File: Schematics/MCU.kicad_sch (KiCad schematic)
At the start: 0 parts

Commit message: Selected MCU
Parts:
- added U?: ATmega32U4-M, Package_DFN_QFN:QFN-44-1EP_7x7mm_P0.5mm_EP5.2x5.2mm, symbol MCU_Microchip_ATmega:ATmega32U4-M
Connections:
- new net: U?.14 (VCC), U?.34 (VCC)
- new net: U?.15 (GND), U?.23 (GND), U?.35 (GND), U?.43 (GND), U?.45 (GND)
- new net: U?.24 (AVCC), U?.44 (AVCC)
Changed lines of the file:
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@@
 (kicad_sch (version 20211123) (generator eeschema)
   (paper "A4")
+  (symbol (lib_id "MCU_Microchip_ATmega:ATmega32U4-M") (at 147.32 101.6 0) (unit 1)
+    (in_bom yes) (on_board yes) (fields_autoplaced)
+    (property "Reference" "U?" (id 0) (at 149.3394 146.9295 0)
+      (effects (font (size 1.27 1.27)) (justify left))
+    )
+    (property "Value" "ATmega32U4-M" (id 1) (at 149.3394 149.7046 0)
+      (effects (font (size 1.27 1.27)) (justify left))
+    )
+    (property "Footprint" "Package_DFN_QFN:QFN-44-1EP_7x7mm_P0.5mm_EP5.2x5.2mm" (id 2) (at 147.32 101.6 0)
+      (effects (font (size 1.27 1.27) italic) hide)
+    )
+    (property "Datasheet" "http://ww1.microchip.com/downloads/en/DeviceDoc/Atmel-7766-8-bit-AVR-ATmega16U4-32U4_Datasheet.pdf" (id 3) (at 147.32 101.6 0)
+      (effects (font (size 1.27 1.27)) hide)
+    )
+    (pin "1")
+    (pin "10")
+    (pin "11")
+    (pin "12")
+    (pin "13")
+    (pin "14")
+    (pin "15")
+    (pin "16")
+    (pin "17")
+    (pin "18")
+    (pin "19")
+    (pin "2")
+    (pin "20")
+    (pin "21")
+    (pin "22")
+    (pin "23")
+    (pin "24")
+    (pin "25")
+    (pin "26")
+    (pin "27")
+    (pin "28")
+    (pin "29")
+    (pin "3")
+    (pin "30")
+    (pin "31")
+    (pin "32")
+    (pin "33")
+    (pin "34")
+    (pin "35")
+    (pin "36")
+    (pin "37")
+    (pin "38")
+    (pin "39")
+    (pin "4")
+    (pin "40")
+    (pin "41")
+    (pin "42")
+    (pin "43")
+    (pin "44")
+    (pin "45")
+    (pin "5")
+    (pin "6")
+    (pin "7")
+    (pin "8")
+    (pin "9")
+  )
 )

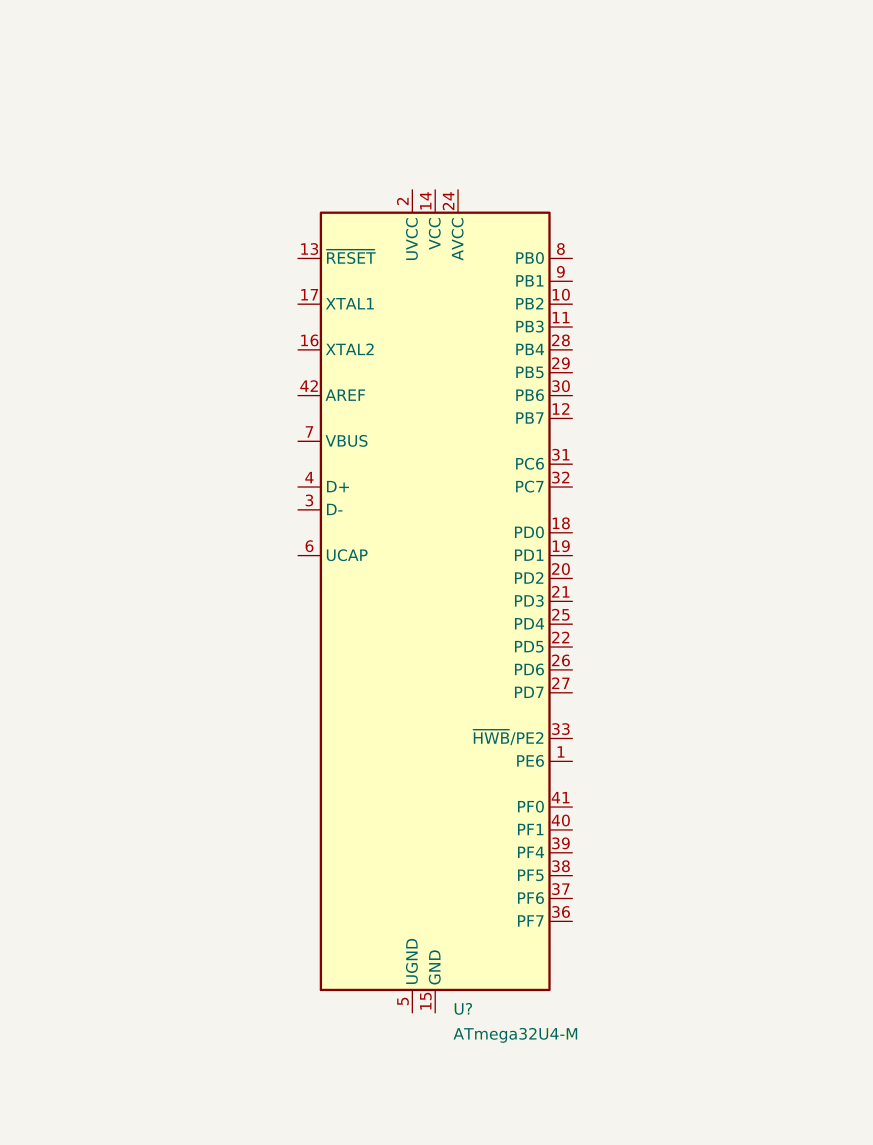
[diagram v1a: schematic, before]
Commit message: Add MCU circuit
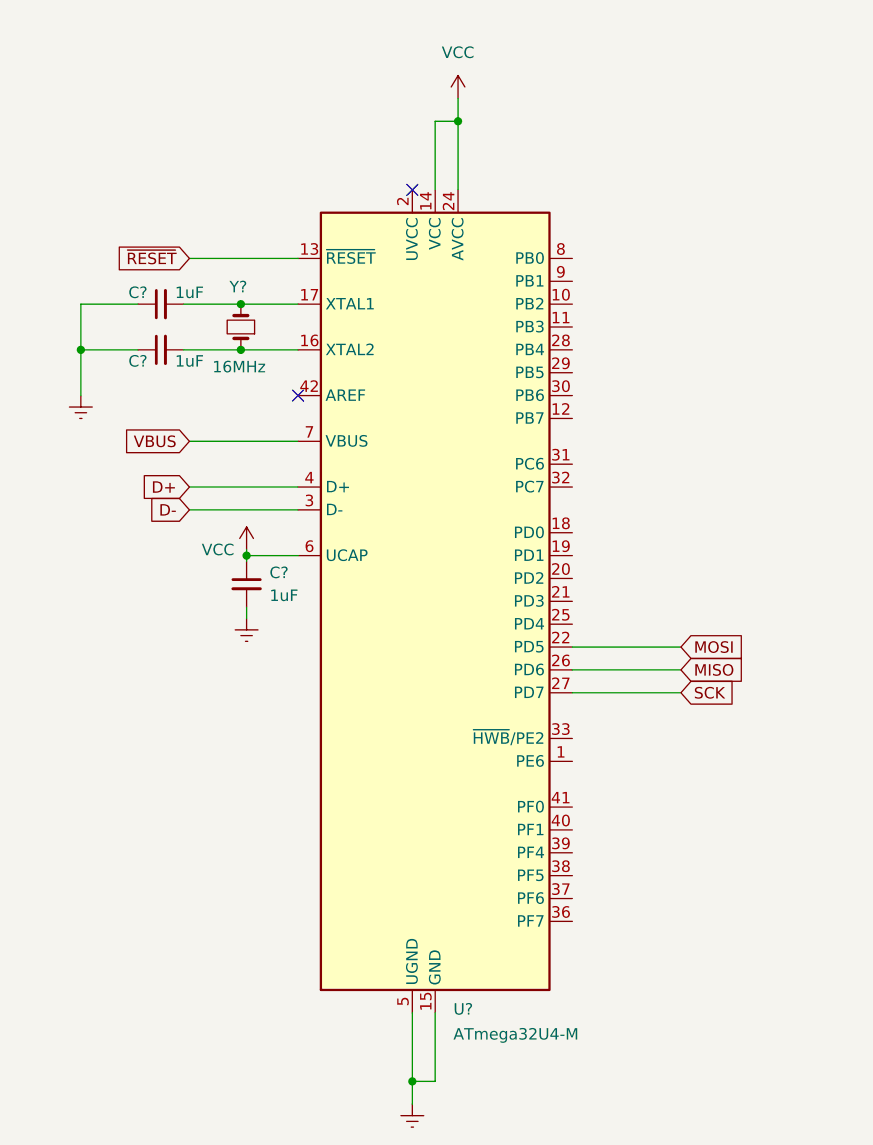
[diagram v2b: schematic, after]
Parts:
- added C? (x3): 1uF, symbol Device:C_Small
- added Y?: 16MHz, symbol Device:Crystal_Small
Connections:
- net ~{RESET}: now reaches U?.13 (~{RESET})
- net VCC: now reaches U?.14 (VCC), U?.34 (VCC)
- net VCC: now also U?.24 (AVCC), U?.44 (AVCC), U?.6 (UCAP), C?.1
- net Earth: now reaches U?.15 (GND), U?.23 (GND), U?.35 (GND), U?.43 (GND), U?.45 (GND)
- net Earth: now also U?.5 (UGND), C?.1, C?.1, C?.2
- net at U?.16 (XTAL2): now also C?.2, Y?.1
- net at U?.17 (XTAL1): now also C?.2, Y?.2
- net MOSI: now reaches U?.22 (PD5)
- net MISO: now reaches U?.26 (PD6)
- net SCK: now reaches U?.27 (PD7)
- net D-: now reaches U?.3 (D-)
- net D+: now reaches U?.4 (D+)
- net VBUS: now reaches U?.7 (VBUS)
- no-connect marks 0 -> 2

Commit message: Changed MCU
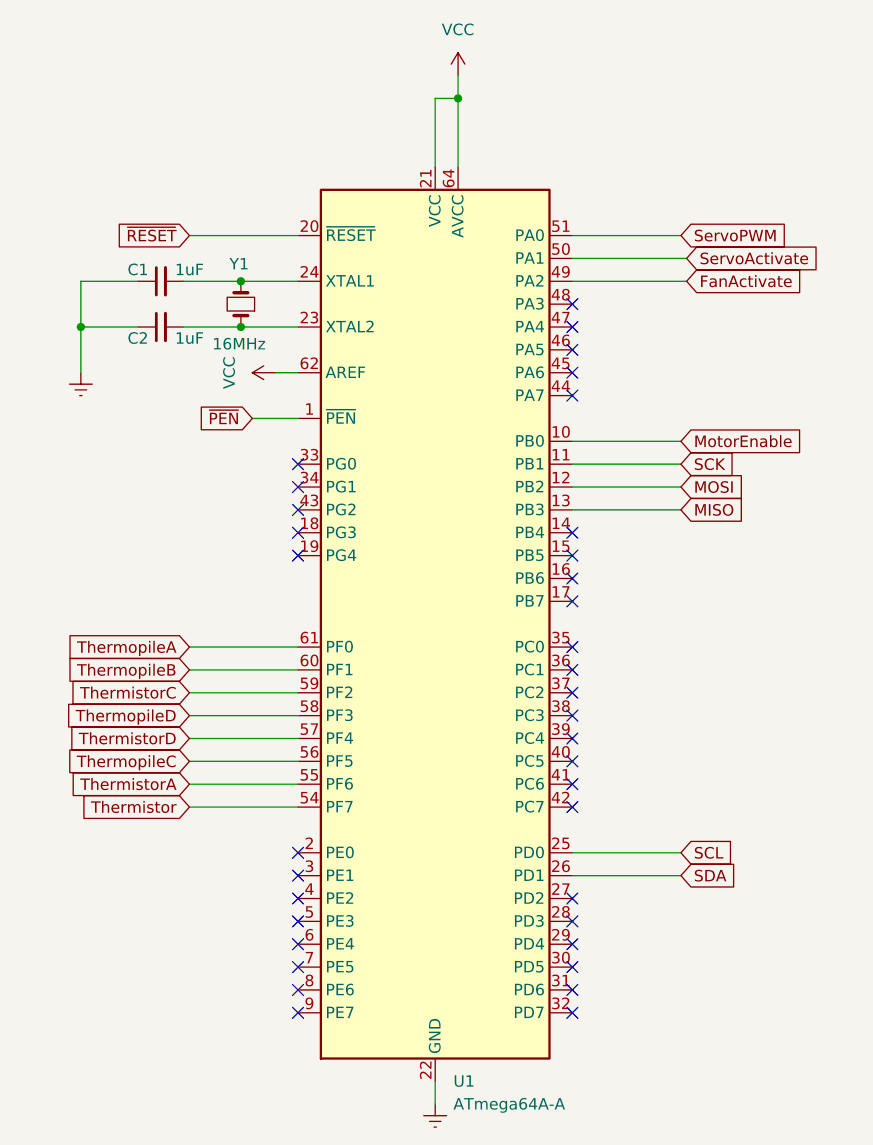
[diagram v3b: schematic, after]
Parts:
- removed C? (x3): 1uF, symbol Device:C_Small
- removed U?: ATmega32U4-M, Package_DFN_QFN:QFN-44-1EP_7x7mm_P0.5mm_EP5.2x5.2mm, symbol MCU_Microchip_ATmega:ATmega32U4-M
- removed Y?: 16MHz, symbol Device:Crystal_Small
- added C1, C2: 1uF, symbol Device:C_Small
- added U1: ATmega64A-A, Package_QFP:TQFP-64_14x14mm_P0.8mm, symbol MCU_Microchip_ATmega:ATmega64A-A
- added Y1: 16MHz, symbol Device:Crystal_Small
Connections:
- net Earth: now also C1.1, C2.1, U1.22 (GND), U1.53 (GND), U1.63 (GND)
- net MISO: now also U1.13 (PB3)
- net MOSI: now also U1.12 (PB2)
- net SCK: now also U1.11 (PB1)
- net VCC: now also U1.21 (VCC), U1.52 (VCC), U1.62 (AREF), U1.64 (AVCC)
- net ~{RESET}: now also U1.20 (~{RESET})
- new net: C2.2, U1.23 (XTAL2), Y1.1
- new net: C1.2, U1.24 (XTAL1), Y1.2
- new net FanActivate: U1.49 (PA2)
- new net MotorEnable: U1.10 (PB0)
- new net SCL: U1.25 (PD0)
- new net SDA: U1.26 (PD1)
- new net ServoActivate: U1.50 (PA1)
- new net ServoPWM: U1.51 (PA0)
- new net Thermistor: U1.54 (PF7)
- new net ThermistorA: U1.55 (PF6)
- new net ThermistorC: U1.59 (PF2)
- new net ThermistorD: U1.57 (PF4)
- new net ThermopileA: U1.61 (PF0)
- new net ThermopileB: U1.60 (PF1)
- new net ThermopileC: U1.56 (PF5)
- new net ThermopileD: U1.58 (PF3)
- new net ~{PEN}: U1.1 (~{PEN})
- no-connect marks 2 -> 36

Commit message: Added Footprints
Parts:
- C1, C2: footprint (none) -> Resistor_SMD:R_0603_1608Metric_Pad0.98x0.95mm_HandSolder
- Y1: footprint (none) -> SFRFootprints:XTAL_ECS-160-S-23A-TR
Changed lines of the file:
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@@
       (effects (font (size 1.27 1.27)) (justify right))
     )
-    (property "Footprint" "" (id 2) (at 125.73 68.58 0)
+    (property "Footprint" "SFRFootprints:XTAL_ECS-160-S-23A-TR" (id 2) (at 125.73 68.58 0)
       (effects (font (size 1.27 1.27)) hide)
     )
@@
     (property "Reference" "C2" (id 0) (at 114.3 72.39 90))
     (property "Value" "1uF" (id 1) (at 120.015 72.39 90))
-    (property "Footprint" "" (id 2) (at 116.84 71.12 0)
+    (property "Footprint" "Resistor_SMD:R_0603_1608Metric_Pad0.98x0.95mm_HandSolder" (id 2) (at 116.84 71.12 0)
       (effects (font (size 1.27 1.27)) hide)
     )
@@
     (property "Reference" "C1" (id 0) (at 114.3 64.77 90))
     (property "Value" "1uF" (id 1) (at 120.015 64.77 90))
-    (property "Footprint" "" (id 2) (at 116.84 66.04 0)
+    (property "Footprint" "Resistor_SMD:R_0603_1608Metric_Pad0.98x0.95mm_HandSolder" (id 2) (at 116.84 66.04 0)
       (effects (font (size 1.27 1.27)) hide)
     )

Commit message: PCB
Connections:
- net ThermistorA is gone; now on net ThermopileB: U1.55 (PF6)
- net Thermistor: now also U1.57 (PF4); no longer U1.54 (PF7)
- net ThermistorC: now also U1.60 (PF1); no longer U1.59 (PF2)
- net ThermistorD: now also U1.61 (PF0); no longer U1.57 (PF4)
- net ThermopileA: now also U1.56 (PF5); no longer U1.61 (PF0)
- net ThermopileB: no longer U1.60 (PF1)
- net ThermopileC: now also U1.59 (PF2); no longer U1.56 (PF5)
- new net ThermistorB: U1.54 (PF7)
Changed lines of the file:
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@@
   (no_connect (at 162.56 68.58))
   (no_connect (at 162.56 71.12))
+  (wire (pts (xy 118.11 109.22) (xy 132.08 109.22))
+    (stroke (width 0) (type default) (color 0 0 0 0))
+  )
   (wire (pts (xy 162.56 88.9) (xy 174.625 88.9))
     (stroke (width 0) (type default) (color 0 0 0 0))
   )
+  (wire (pts (xy 118.11 106.68) (xy 132.08 106.68))
+    (stroke (width 0) (type default) (color 0 0 0 0))
+  )
   (wire (pts (xy 107.95 71.12) (xy 107.95 76.2))
     (stroke (width 0) (type default) (color 0 0 0 0))
@@
     (stroke (width 0) (type default) (color 0 0 0 0))
   )
-  (wire (pts (xy 120.015 109.22) (xy 132.08 109.22))
-    (stroke (width 0) (type default) (color 0 0 0 0))
-  )
   (wire (pts (xy 127 81.28) (xy 132.08 81.28))
     (stroke (width 0) (type default) (color 0 0 0 0))
   )
-  (wire (pts (xy 120.015 114.3) (xy 132.08 114.3))
-    (stroke (width 0) (type default) (color 0 0 0 0))
-  )
   (wire (pts (xy 149.86 45.72) (xy 147.32 45.72))
     (stroke (width 0) (type default) (color 0 0 0 0))
   )
+  (wire (pts (xy 118.11 111.76) (xy 132.08 111.76))
+    (stroke (width 0) (type default) (color 0 0 0 0))
+  )
   (wire (pts (xy 125.73 71.12) (xy 132.08 71.12))
     (stroke (width 0) (type default) (color 0 0 0 0))
@@
     (stroke (width 0) (type default) (color 0 0 0 0))
   )
-  (wire (pts (xy 120.015 111.76) (xy 132.08 111.76))
-    (stroke (width 0) (type default) (color 0 0 0 0))
-  )
-  (wire (pts (xy 120.015 119.38) (xy 132.08 119.38))
-    (stroke (width 0) (type default) (color 0 0 0 0))
-  )
   (wire (pts (xy 149.86 53.34) (xy 149.86 45.72))
     (stroke (width 0) (type default) (color 0 0 0 0))
   )
-  (wire (pts (xy 120.015 124.46) (xy 132.08 124.46))
-    (stroke (width 0) (type default) (color 0 0 0 0))
-  )
   (wire (pts (xy 162.56 91.44) (xy 174.625 91.44))
     (stroke (width 0) (type default) (color 0 0 0 0))
@@
     (stroke (width 0) (type default) (color 0 0 0 0))
   )
-  (wire (pts (xy 120.015 121.92) (xy 132.08 121.92))
-    (stroke (width 0) (type default) (color 0 0 0 0))
-  )
   (wire (pts (xy 162.56 66.04) (xy 175.26 66.04))
     (stroke (width 0) (type default) (color 0 0 0 0))
@@
     (stroke (width 0) (type default) (color 0 0 0 0))
   )
+  (wire (pts (xy 118.11 119.38) (xy 132.08 119.38))
+    (stroke (width 0) (type default) (color 0 0 0 0))
+  )
   (wire (pts (xy 119.38 66.04) (xy 125.73 66.04))
     (stroke (width 0) (type default) (color 0 0 0 0))
   )
-  (wire (pts (xy 120.015 116.84) (xy 132.08 116.84))
+  (wire (pts (xy 118.11 114.3) (xy 132.08 114.3))
+    (stroke (width 0) (type default) (color 0 0 0 0))
+  )
+  (wire (pts (xy 118.11 116.84) (xy 132.08 116.84))
     (stroke (width 0) (type default) (color 0 0 0 0))
   )
@@
     (stroke (width 0) (type default) (color 0 0 0 0))
   )
-  (wire (pts (xy 120.015 106.68) (xy 132.08 106.68))
+  (wire (pts (xy 118.11 124.46) (xy 132.08 124.46))
+    (stroke (width 0) (type default) (color 0 0 0 0))
+  )
+  (wire (pts (xy 118.11 121.92) (xy 132.08 121.92))
     (stroke (width 0) (type default) (color 0 0 0 0))
   )
@@
     (stroke (width 0) (type default) (color 0 0 0 0))
   )
-  (global_label "ThermistorD" (shape input) (at 120.015 116.84 180) (fields_autoplaced)
-    (effects (font (size 1.27 1.27)) (justify right))
-    (property "Intersheet References" "${INTERSHEET_REFS}" (id 0) (at 106.3533 116.9194 0)
+  (global_label "ThermistorD" (shape input) (at 118.11 106.68 180) (fields_autoplaced)
+    (effects (font (size 1.27 1.27)) (justify right))
+    (property "Intersheet References" "${INTERSHEET_REFS}" (id 0) (at 104.4483 106.7594 0)
       (effects (font (size 1.27 1.27)) (justify right) hide)
     )
@@
     )
   )
-  (global_label "ThermopileC" (shape input) (at 120.015 119.38 180) (fields_autoplaced)
-    (effects (font (size 1.27 1.27)) (justify right))
-    (property "Intersheet References" "${INTERSHEET_REFS}" (id 0) (at 105.9905 119.4594 0)
+  (global_label "ThermopileC" (shape input) (at 118.11 111.76 180) (fields_autoplaced)
+    (effects (font (size 1.27 1.27)) (justify right))
+    (property "Intersheet References" "${INTERSHEET_REFS}" (id 0) (at 104.0855 111.8394 0)
       (effects (font (size 1.27 1.27)) (justify right) hide)
     )
@@
     )
   )
-  (global_label "ThermopileA" (shape input) (at 120.015 106.68 180) (fields_autoplaced)
-    (effects (font (size 1.27 1.27)) (justify right))
-    (property "Intersheet References" "${INTERSHEET_REFS}" (id 0) (at 106.1719 106.7594 0)
-      (effects (font (size 1.27 1.27)) (justify right) hide)
-    )
-  )
   (global_label "ServoPWM" (shape input) (at 174.625 60.96 0) (fields_autoplaced)
     (effects (font (size 1.27 1.27)) (justify left))
@@
     )
   )
+  (global_label "ThermopileB" (shape input) (at 118.11 121.92 180) (fields_autoplaced)
+    (effects (font (size 1.27 1.27)) (justify right))
+    (property "Intersheet References" "${INTERSHEET_REFS}" (id 0) (at 104.0855 121.8406 0)
+      (effects (font (size 1.27 1.27)) (justify right) hide)
+    )
+  )
   (global_label "~{RESET}" (shape input) (at 120.015 60.96 180) (fields_autoplaced)
     (effects (font (size 1.27 1.27)) (justify right))
@@
     )
   )
-  (global_label "ThermistorC" (shape input) (at 120.015 111.76 180) (fields_autoplaced)
-    (effects (font (size 1.27 1.27)) (justify right))
-    (property "Intersheet References" "${INTERSHEET_REFS}" (id 0) (at 106.3533 111.6806 0)
-      (effects (font (size 1.27 1.27)) (justify right) hide)
-    )
-  )
-  (global_label "ThermopileD" (shape input) (at 120.015 114.3 180) (fields_autoplaced)
-    (effects (font (size 1.27 1.27)) (justify right))
-    (property "Intersheet References" "${INTERSHEET_REFS}" (id 0) (at 105.9905 114.2206 0)
-      (effects (font (size 1.27 1.27)) (justify right) hide)
-    )
-  )
-  (global_label "ThermistorA" (shape input) (at 120.015 121.92 180) (fields_autoplaced)
-    (effects (font (size 1.27 1.27)) (justify right))
-    (property "Intersheet References" "${INTERSHEET_REFS}" (id 0) (at 106.5348 121.8406 0)
+  (global_label "ThermistorC" (shape input) (at 118.11 109.22 180) (fields_autoplaced)
+    (effects (font (size 1.27 1.27)) (justify right))
+    (property "Intersheet References" "${INTERSHEET_REFS}" (id 0) (at 104.4483 109.1406 0)
+      (effects (font (size 1.27 1.27)) (justify right) hide)
+    )
+  )
+  (global_label "ThermopileD" (shape input) (at 118.11 114.3 180) (fields_autoplaced)
+    (effects (font (size 1.27 1.27)) (justify right))
+    (property "Intersheet References" "${INTERSHEET_REFS}" (id 0) (at 104.0855 114.2206 0)
+      (effects (font (size 1.27 1.27)) (justify right) hide)
+    )
+  )
+  (global_label "ThermistorB" (shape input) (at 118.11 124.46 180) (fields_autoplaced)
+    (effects (font (size 1.27 1.27)) (justify right))
+    (property "Intersheet References" "${INTERSHEET_REFS}" (id 0) (at 104.4483 124.3806 0)
       (effects (font (size 1.27 1.27)) (justify right) hide)
     )
@@
     )
   )
+  (global_label "ThermopileA" (shape input) (at 118.11 119.38 180) (fields_autoplaced)
+    (effects (font (size 1.27 1.27)) (justify right))
+    (property "Intersheet References" "${INTERSHEET_REFS}" (id 0) (at 104.2669 119.4594 0)
+      (effects (font (size 1.27 1.27)) (justify right) hide)
+    )
+  )
   (global_label "SCK" (shape input) (at 174.625 86.36 0) (fields_autoplaced)
     (effects (font (size 1.27 1.27)) (justify left))
@@
     )
   )
-  (global_label "ThermopileB" (shape input) (at 120.015 109.22 180) (fields_autoplaced)
-    (effects (font (size 1.27 1.27)) (justify right))
-    (property "Intersheet References" "${INTERSHEET_REFS}" (id 0) (at 105.9905 109.1406 0)
-      (effects (font (size 1.27 1.27)) (justify right) hide)
-    )
-  )
   (global_label "MOSI" (shape input) (at 174.625 88.9 0) (fields_autoplaced)
     (effects (font (size 1.27 1.27)) (justify left))
@@
     )
   )
-  (global_label "Thermistor" (shape input) (at 120.015 124.46 180) (fields_autoplaced)
-    (effects (font (size 1.27 1.27)) (justify right))
-    (property "Intersheet References" "${INTERSHEET_REFS}" (id 0) (at 107.6233 124.3806 0)
-      (effects (font (size 1.27 1.27)) (justify right) hide)
-    )
+  (global_label "Thermistor" (shape input) (at 118.11 116.84 180) (fields_autoplaced)
+    (effects (font (size 1.27 1.27)) (justify right))
+    (property "Intersheet References" "${INTERSHEET_REFS}" (id 0) (at 105.7183 116.7606 0)
+      (effects (font (size 1.27 1.27)) (justify right) hide)
+    )

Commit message: PCB
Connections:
- net FanActivate: now also U1.50 (PA1); no longer U1.49 (PA2)
- net ServoActivate: now also U1.49 (PA2); no longer U1.50 (PA1)
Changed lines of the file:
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@@
     )
   )
-  (global_label "ServoActivate" (shape input) (at 175.26 63.5 0) (fields_autoplaced)
+  (global_label "ServoActivate" (shape input) (at 175.26 66.04 0) (fields_autoplaced)
     (effects (font (size 1.27 1.27)) (justify left))
-    (property "Intersheet References" "${INTERSHEET_REFS}" (id 0) (at 190.3126 63.4206 0)
+    (property "Intersheet References" "${INTERSHEET_REFS}" (id 0) (at 190.3126 65.9606 0)
       (effects (font (size 1.27 1.27)) (justify left) hide)
     )
@@
     )
   )
-  (global_label "FanActivate" (shape input) (at 175.26 66.04 0) (fields_autoplaced)
+  (global_label "FanActivate" (shape input) (at 175.26 63.5 0) (fields_autoplaced)
     (effects (font (size 1.27 1.27)) (justify left))
-    (property "Intersheet References" "${INTERSHEET_REFS}" (id 0) (at 188.4983 65.9606 0)
+    (property "Intersheet References" "${INTERSHEET_REFS}" (id 0) (at 188.4983 63.4206 0)
       (effects (font (size 1.27 1.27)) (justify left) hide)
     )
